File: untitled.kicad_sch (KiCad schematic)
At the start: 18 parts, among them J1 Raspberry_Pi_40pin, J12 Conn_01x03_Pin, J3 Conn_02x06_Odd_Even, P1 USB_C_Receptacle_USB2.0, U4 BC847BDW1T1G, U5 CP2102N-A02-GQFN28

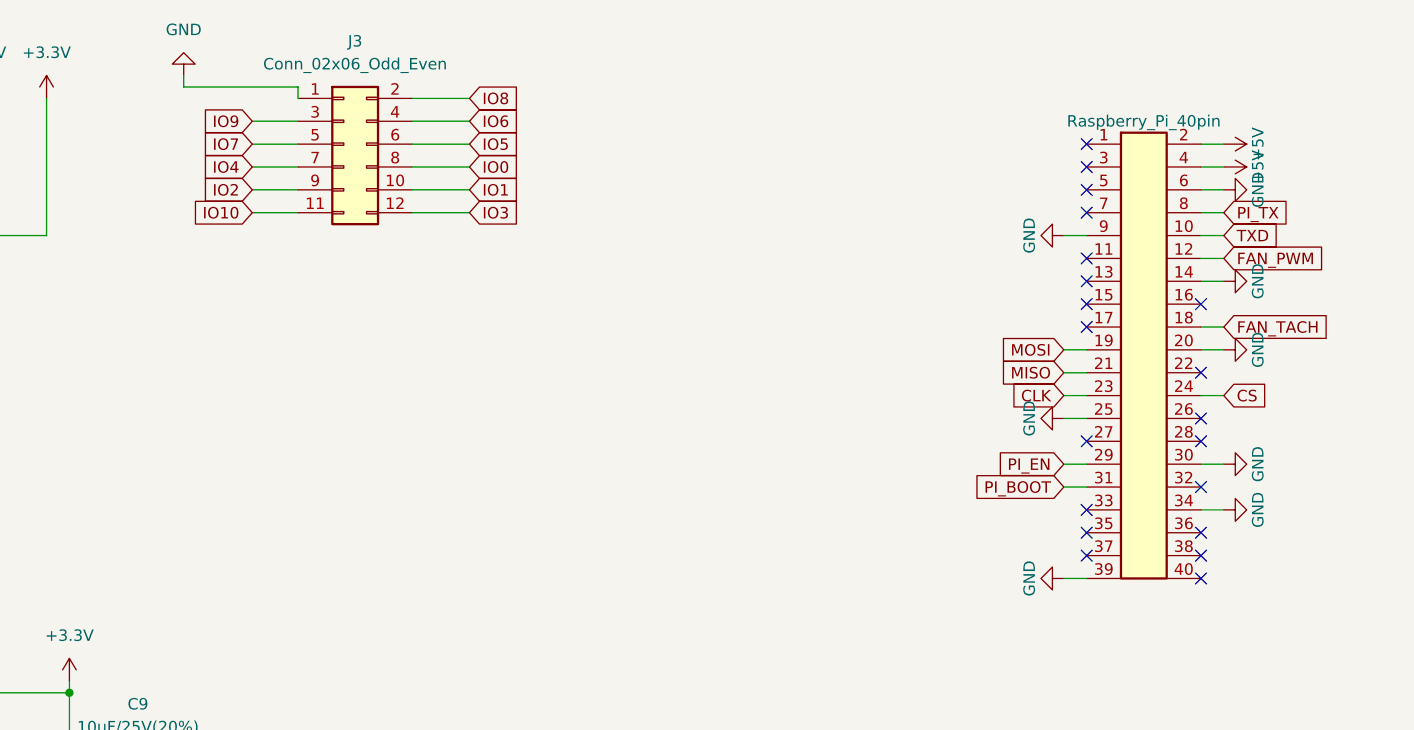
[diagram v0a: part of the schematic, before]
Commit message: Place decoupling caps, remove fan circuit and J3, add spare ESP32-Pi lines
Schematic:
- Remove the fan circuit (J13, Q1, D8, R31-R33, TP15-17); the Pi 5 drives
  its own Active Cooler. J1 pins 12/18 are now no-connect
- Remove the J3 debug header; J1 doubles as the dev header without a Pi
- IO0/IO1 to J1 pins 37/36 (Pi GPIO26/16) through R37/R38 1k as spare lines

Board:
- Test points moved to the bottom side to free space on top
- Decoupling caps C2/C3/C5/C8/C16/C18-C21 and R35/R36 placed next to
  their ICs; U8 nudged and R23/R10 moved to make room
- Conflicting tracks ripped up and rerouted; 6 connections left for
  interactive routing
- Back pinout table updated (fan and J3 rows replaced by J1 37/36)
- Courtyard exception rule for caps inside their IC's courtyard margin
- DRC (JLCPCB rules): 0 errors; ERC: 0 errors; schematic parity clean

Co-Authored-By: Claude Opus 5.5 <noreply@anthropic.com>
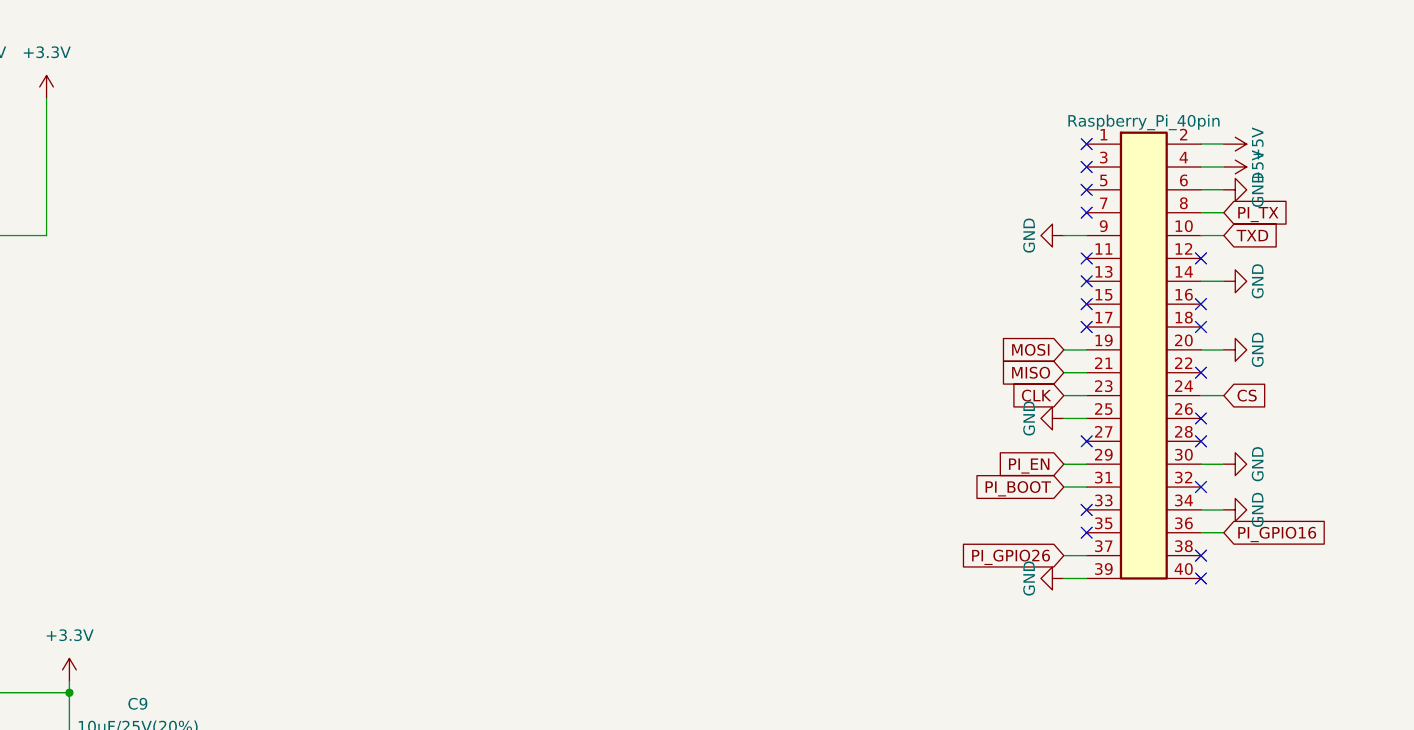
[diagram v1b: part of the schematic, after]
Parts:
- removed J3: Conn_02x06_Odd_Even, Connector_PinHeader_2.54mm:PinHeader_2x06_P2.54mm_Vertical, symbol Connector_Generic:Conn_02x06_Odd_Even
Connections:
- net PI_GPIO16: now reaches J1.36 (Pin_36)
- net PI_GPIO26: now reaches J1.37 (Pin_37)
- net FAN_PWM: no longer names the net of J1.12 (Pin_12)
- net FAN_TACH: no longer names the net of J1.18 (Pin_18)

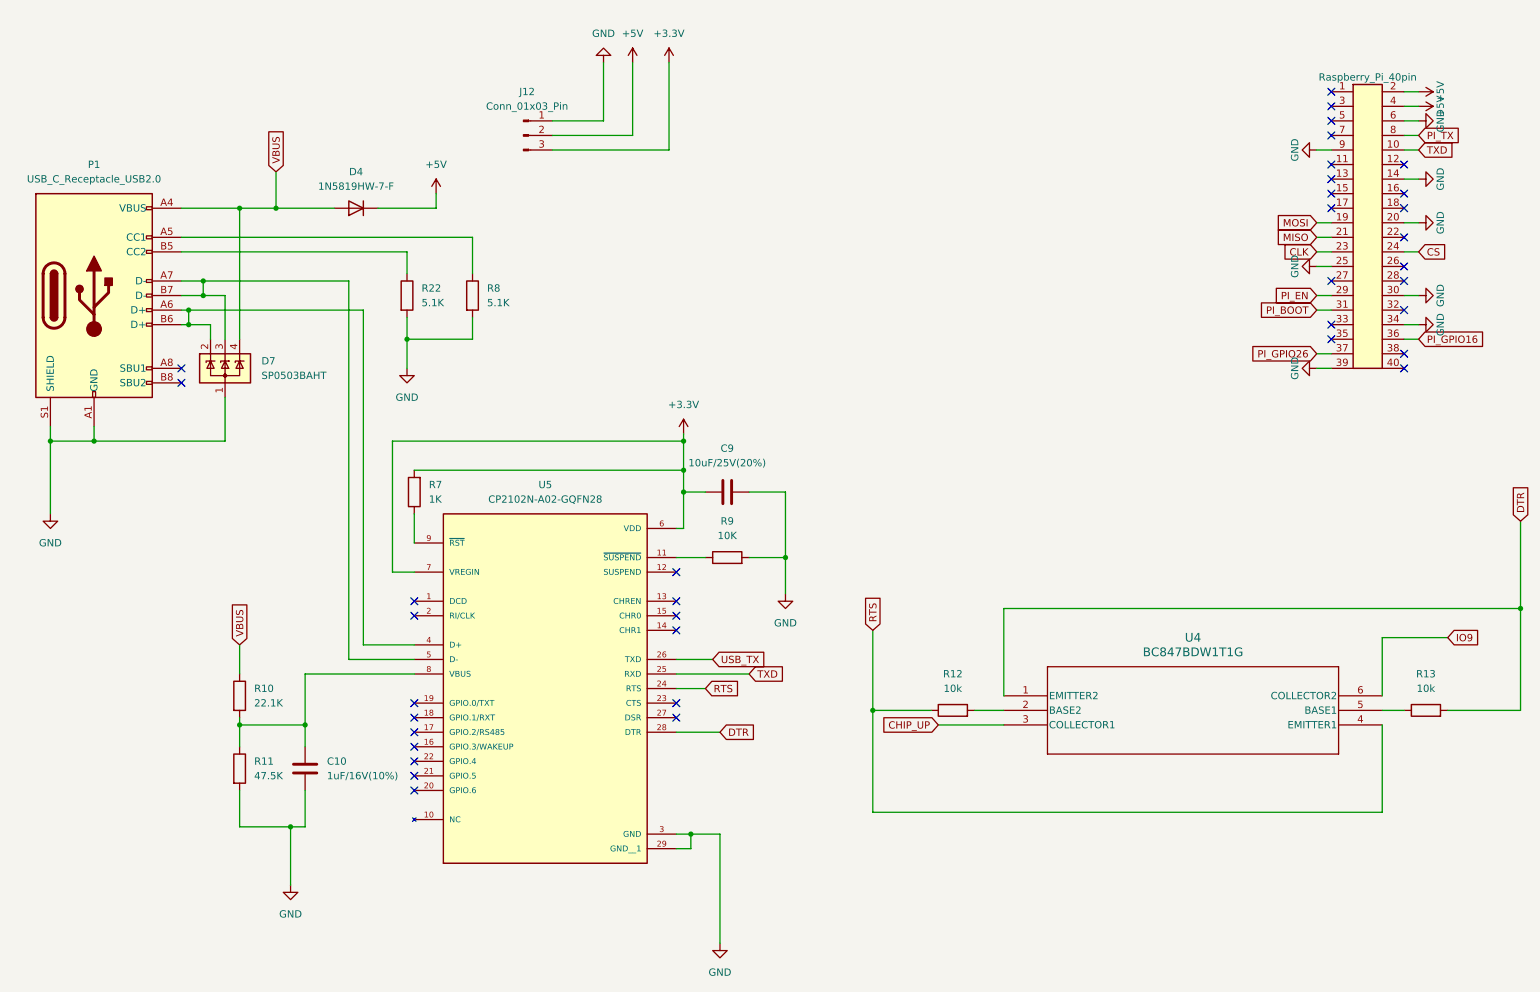
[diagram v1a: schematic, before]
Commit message: Test board schematic: bare ESP32-C3FH4, native USB, noise fixes
A - bare chip (docs/esp32-c3-chip-design.md):
- ESP32-C3FH4 (4 MB in-package flash) replaces the WROOM-02 module
- Espressif reference core: VDD3P3 2.0 nH filter + 1 uF, VDDA 1 uF + 10 nF,
  RTC/CPU 100 nF, VDD_SPI 1 uF, 40 MHz crystal with 24 nH series and 22 pF
- RF: CLC match at the chip, pi footprint with 6.8 nH at a Walsin
  RFANT3216120A5T chip antenna (shunts DNP for tuning)
- 499 ohm on U0TXD

B - native USB:
- USB-C D+/D- via ESD and 22 ohm to GPIO19/18 (USB Serial/JTAG);
  D+ pull-up footprint DNP
- CP2102N, DTR/RTS auto-reset and the UART AND gate removed; J1 pin 8
  drives ESP32 RX directly (R27 pull-up)

Noise fixes (docs/noise-analysis-v4.md):
- 10k pull-downs and SRV05-4 TVS arrays on CH1-CH8
- SMBJ5.0A TVS on +5V, 100 uF at J1, 3 x 100 nF spread on +5V

ERC: 0 errors. Board layout not updated yet.

Co-Authored-By: Claude Opus 5.5 <noreply@anthropic.com>
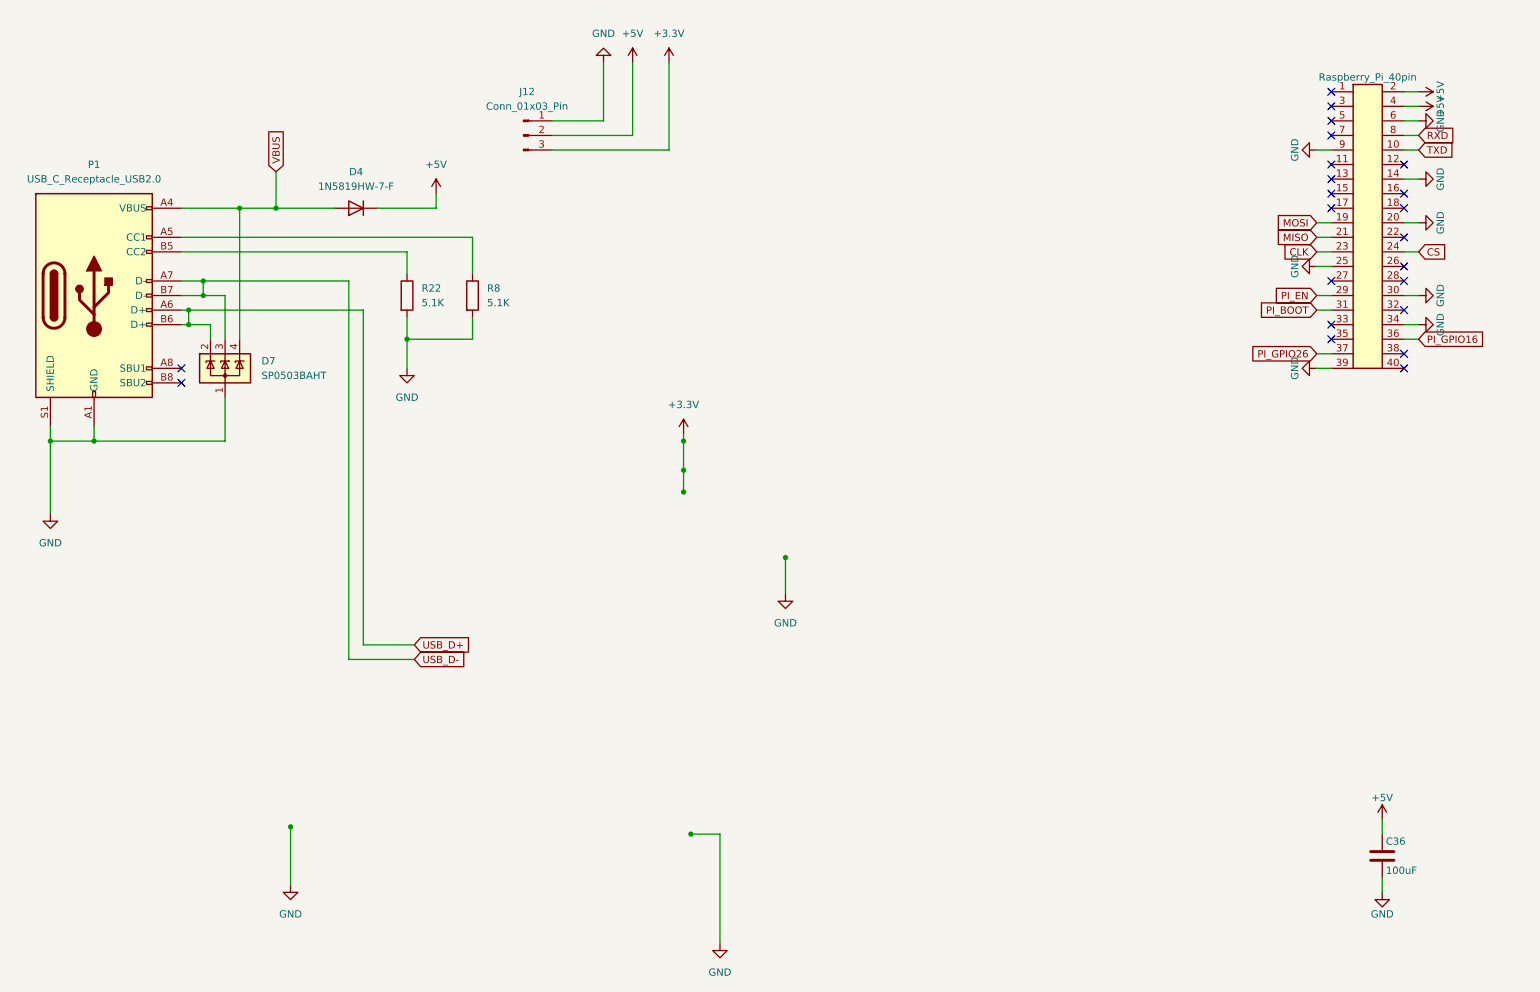
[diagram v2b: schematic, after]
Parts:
- removed C10: 1uF/16V(10%), Capacitor_SMD:C_0603_1608Metric, symbol Device:C
- removed C9: 10uF/25V(20%), Capacitor_SMD:C_0603_1608Metric, symbol Device:C
- removed R10: 22.1K, Resistor_SMD:R_0603_1608Metric, symbol Device:R
- removed R11: 47.5K, Resistor_SMD:R_0603_1608Metric, symbol Device:R
- removed R12, R13: 10k, Resistor_SMD:R_0603_1608Metric, symbol Device:R
- removed R7: 1K, Resistor_SMD:R_0603_1608Metric, symbol Device:R
- removed R9: 10K, Resistor_SMD:R_0603_1608Metric, symbol Device:R
- removed U4: BC847BDW1T1G, Transistor_Power_Module:SOT65P210X110-6N, symbol Transistor_Array:BC847BDW1T1G
- removed U5: CP2102N-A02-GQFN28, Connector_USB:QFN50P500X500X80-29N, symbol Interface_USB:CP2102N-A02-GQFN28
- added C36: 100uF, Capacitor_SMD:C_1210_3225Metric, symbol Device:C
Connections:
- net +5V: now also C36.1
- net GND: now also C36.2
- net USB_D+: now reaches D7.2 (K), P1.A6 (D+), P1.B6 (D+)
- net USB_D-: now reaches D7.3 (K), P1.A7 (D-), P1.B7 (D-)
- net PI_TX renamed RXD
- no-connect marks 37 -> 22

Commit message: Test board: move protection parts and C36, reroute USB away from LEDs
- C36 (Pi bulk) now 100uF 1206, 5 mm from J1 pins 2/4 (was 39 mm).
- U11 next to the J4-J7 column, U12 below the V_IN terminals, D10 closer to V_IN.
- R40 beside R39 under U1; USB D+/D- rerouted below the JST block.
- CH nets rerouted; maze now checks every layer when placing vias.
- Noise analysis updated with the re-measured values.

Co-Authored-By: Claude Opus 5.5 <noreply@anthropic.com>
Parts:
- C36: footprint Capacitor_SMD:C_1210_3225Metric -> Capacitor_SMD:C_1206_3216Metric
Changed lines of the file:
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@@
       (effects (font (size 1.27 1.27)) (justify left))
     )
-    (property "Footprint" "Capacitor_SMD:C_1210_3225Metric" (at 252.4252 168.91 0)
+    (property "Footprint" "Capacitor_SMD:C_1206_3216Metric" (at 252.4252 168.91 0)
       (effects (font (size 1.27 1.27)) hide)
     )

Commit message: R42 -> 510R (C25123) and D4 -> B5819W (C8598), both JLC Basic parts
Saves two extended-part setup fees. Same footprints; JLC rotation and
polarity checked (CPL unchanged).

Co-Authored-By: Claude Opus 5.5 <noreply@anthropic.com>
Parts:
- D4: value 1N5819HW-7-F -> B5819W
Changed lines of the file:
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@@
       (effects (font (size 1.27 1.27)))
     )
-    (property "Value" "1N5819HW-7-F" (at 72.39 48.26 0)
+    (property "Value" "B5819W" (at 72.39 48.26 0)
       (effects (font (size 1.27 1.27)))
     )
